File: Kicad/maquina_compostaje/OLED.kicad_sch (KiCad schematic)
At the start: 1 part, among them J8 Conn_01x04

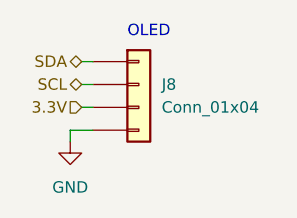
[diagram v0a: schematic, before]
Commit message: se agregaron componentes en la parte inferior de la placa
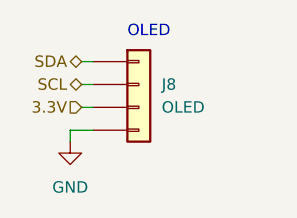
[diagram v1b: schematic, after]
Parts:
- J8: value Conn_01x04 -> OLED
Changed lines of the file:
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@@
       (effects (font (size 1.27 1.27)) (justify left))
     )
-    (property "Value" "Conn_01x04" (id 1) (at 43.18 33.0199 0)
+    (property "Value" "OLED" (id 1) (at 43.18 33.0199 0)
       (effects (font (size 1.27 1.27)) (justify left))
     )
